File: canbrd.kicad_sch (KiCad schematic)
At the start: 5 parts

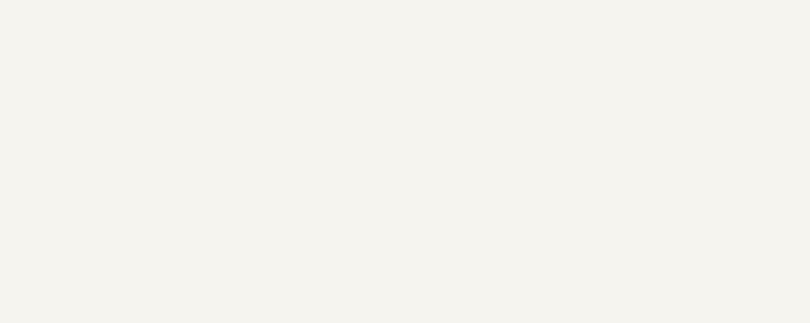
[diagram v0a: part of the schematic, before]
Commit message: rev1.1: Add I2C pullups
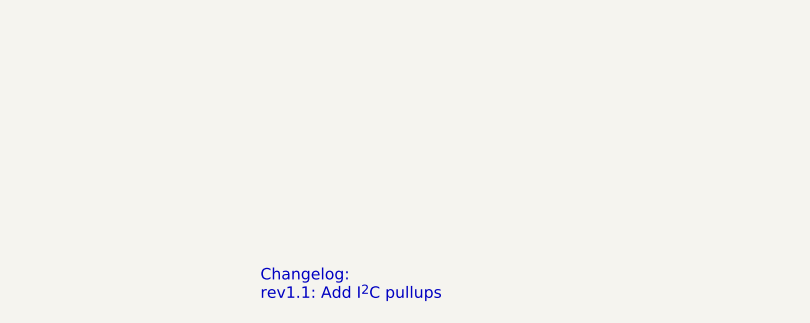
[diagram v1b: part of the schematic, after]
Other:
- note added: "Changelog: rev1.1: Add I^{2}C pullups"
